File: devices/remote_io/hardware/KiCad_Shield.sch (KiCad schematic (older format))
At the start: 72 parts, among them IC1 ATECC508A, J1 Conn_01x04_Male, P1 Power, P2 Analog, P3 Digital, P4 Digital, P5 CONN_1, P6 CONN_1, P7 CONN_1, P8 CONN_1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

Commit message: Added JLCPCB
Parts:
- D1, D2, D3, D4: LCSC (none) -> C397049
- Q1, Q3: LCSC (none) -> C82045
- Q2, Q4: LCSC (none) -> C411721
- R1, R10, R2, R3, R4, R5, R6, R7, R8, R9: LCSC (none) -> C21189
- R11, R12, R13, R14, R28, R30, R31, R34, R36, R38, R40, R42, R45, R46, R48, R49, R50, R52: LCSC (none) -> C25804
- R21, R22, R23, R24: LCSC (none) -> C21190
- R47, R51: LCSC (none) -> C4190
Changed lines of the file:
@@
 EESchema Schematic File Version 4
-LIBS:KiCad_Shield-cache
 EELAYER 30 0
 EELAYER END
@@
 F 2 "Resistor_SMD:R_0603_1608Metric" V 6830 1900 50  0001 C CNN
 F 3 "" H 6900 1900 50  0000 C CNN
+F 4 "C25804" V 6900 1900 50  0001 C CNN "LCSC"
 	1    6900 1900
 	0    1    1    0
@@
 F 2 "Resistor_SMD:R_0603_1608Metric" V 6830 2500 50  0001 C CNN
 F 3 "" H 6900 2500 50  0000 C CNN
+F 4 "C25804" V 6900 2500 50  0001 C CNN "LCSC"
 	1    6900 2500
 	0    1    1    0
@@
 F 2 "Resistor_SMD:R_0603_1608Metric" V 6830 2900 50  0001 C CNN
 F 3 "" H 6900 2900 50  0000 C CNN
+F 4 "C25804" V 6900 2900 50  0001 C CNN "LCSC"
 	1    6900 2900
 	0    1    1    0
@@
 F 2 "Resistor_SMD:R_0603_1608Metric" V 6830 3750 50  0001 C CNN
 F 3 "" H 6900 3750 50  0000 C CNN
+F 4 "C25804" V 6900 3750 50  0001 C CNN "LCSC"
 	1    6900 3750
 	0    1    1    0
@@
 F 2 "Resistor_SMD:R_0603_1608Metric" V 6830 4350 50  0001 C CNN
 F 3 "" H 6900 4350 50  0000 C CNN
+F 4 "C25804" V 6900 4350 50  0001 C CNN "LCSC"
 	1    6900 4350
 	0    1    1    0
@@
 F 2 "Resistor_SMD:R_0603_1608Metric" V 6830 4950 50  0001 C CNN
 F 3 "" H 6900 4950 50  0000 C CNN
+F 4 "C25804" V 6900 4950 50  0001 C CNN "LCSC"
 	1    6900 4950
 	0    1    1    0
@@
 F 2 "Resistor_SMD:R_0603_1608Metric" V 6830 5600 50  0001 C CNN
 F 3 "" H 6900 5600 50  0000 C CNN
+F 4 "C25804" V 6900 5600 50  0001 C CNN "LCSC"
 	1    6900 5600
 	0    1    1    0
@@
 F 2 "Resistor_SMD:R_0603_1608Metric" V 6830 6200 50  0001 C CNN
 F 3 "" H 6900 6200 50  0000 C CNN
+F 4 "C25804" V 6900 6200 50  0001 C CNN "LCSC"
 	1    6900 6200
 	0    1    1    0
@@
 F 2 "Resistor_SMD:R_0603_1608Metric" V 2830 2300 50  0001 C CNN
 F 3 "" H 2900 2300 50  0000 C CNN
+F 4 "C21189" V 2900 2300 50  0001 C CNN "LCSC"
 	1    2900 2300
 	0    1    1    0
@@
 F 2 "Resistor_SMD:R_0603_1608Metric" V 2830 2200 50  0001 C CNN
 F 3 "" H 2900 2200 50  0000 C CNN
+F 4 "C21189" V 2900 2200 50  0001 C CNN "LCSC"
 	1    2900 2200
 	0    1    1    0
@@
 F 2 "Resistor_SMD:R_0603_1608Metric" V 2830 2100 50  0001 C CNN
 F 3 "" H 2900 2100 50  0000 C CNN
+F 4 "C21189" V 2900 2100 50  0001 C CNN "LCSC"
 	1    2900 2100
 	0    1    1    0
@@
 F 2 "Resistor_SMD:R_0603_1608Metric" V 2830 2000 50  0001 C CNN
 F 3 "" H 2900 2000 50  0000 C CNN
+F 4 "C21189" V 2900 2000 50  0001 C CNN "LCSC"
 	1    2900 2000
 	0    1    1    0
@@
 F 2 "Resistor_SMD:R_0603_1608Metric" V 2830 1900 50  0001 C CNN
 F 3 "" H 2900 1900 50  0000 C CNN
+F 4 "C21189" V 2900 1900 50  0001 C CNN "LCSC"
 	1    2900 1900
 	0    1    1    0
@@
 F 2 "Resistor_SMD:R_0603_1608Metric" V 2830 1800 50  0001 C CNN
 F 3 "" H 2900 1800 50  0000 C CNN
+F 4 "C21189" V 2900 1800 50  0001 C CNN "LCSC"
 	1    2900 1800
 	0    1    1    0
@@
 F 2 "Resistor_SMD:R_0603_1608Metric" V 2830 1700 50  0001 C CNN
 F 3 "" H 2900 1700 50  0000 C CNN
+F 4 "C21189" V 2900 1700 50  0001 C CNN "LCSC"
 	1    2900 1700
 	0    1    1    0
@@
 F 2 "Resistor_SMD:R_0603_1608Metric" V 2830 1600 50  0001 C CNN
 F 3 "" H 2900 1600 50  0000 C CNN
+F 4 "C21189" V 2900 1600 50  0001 C CNN "LCSC"
 	1    2900 1600
 	0    1    1    0
@@
 F 2 "Resistor_SMD:R_0603_1608Metric" V 2830 1500 50  0001 C CNN
 F 3 "" H 2900 1500 50  0000 C CNN
+F 4 "C21189" V 2900 1500 50  0001 C CNN "LCSC"
 	1    2900 1500
 	0    1    1    0
@@
 F 2 "Resistor_SMD:R_0603_1608Metric" V 2830 1400 50  0001 C CNN
 F 3 "" H 2900 1400 50  0000 C CNN
+F 4 "C21189" V 2900 1400 50  0001 C CNN "LCSC"
 	1    2900 1400
 	0    1    1    0
@@
 F 2 "LED_SMD:LED_0603_1608Metric" H 9000 5750 50  0001 C CNN
 F 3 "~" H 9000 5750 50  0001 C CNN
+F 4 "C397049" V 9000 5750 50  0001 C CNN "LCSC"
 	1    9000 5750
 	0    -1   -1   0
@@
 F 2 "Resistor_SMD:R_0603_1608Metric_Pad1.05x0.95mm_HandSolder" V 8930 5350 50  0001 C CNN
 F 3 "" H 9000 5350 50  0000 C CNN
+F 4 "C21190" V 9000 5350 50  0001 C CNN "LCSC"
 	1    9000 5350
 	-1   0    0    1
@@
 F 2 "LED_SMD:LED_0603_1608Metric" H 9400 5750 50  0001 C CNN
 F 3 "~" H 9400 5750 50  0001 C CNN
+F 4 "C397049" V 9400 5750 50  0001 C CNN "LCSC"
 	1    9400 5750
 	0    -1   -1   0
@@
 F 2 "Resistor_SMD:R_0603_1608Metric_Pad1.05x0.95mm_HandSolder" V 9330 5350 50  0001 C CNN
 F 3 "" H 9400 5350 50  0000 C CNN
+F 4 "C21190" V 9400 5350 50  0001 C CNN "LCSC"
 	1    9400 5350
 	-1   0    0    1
@@
 F 2 "LED_SMD:LED_0603_1608Metric" H 9750 5750 50  0001 C CNN
 F 3 "~" H 9750 5750 50  0001 C CNN
+F 4 "C397049" V 9750 5750 50  0001 C CNN "LCSC"
 	1    9750 5750
 	0    -1   -1   0
@@
 F 2 "Resistor_SMD:R_0603_1608Metric_Pad1.05x0.95mm_HandSolder" V 9680 5350 50  0001 C CNN
 F 3 "" H 9750 5350 50  0000 C CNN
+F 4 "C21190" V 9750 5350 50  0001 C CNN "LCSC"
 	1    9750 5350
 	-1   0    0    1
@@
 F 2 "LED_SMD:LED_0603_1608Metric" H 10150 5750 50  0001 C CNN
 F 3 "~" H 10150 5750 50  0001 C CNN
+F 4 "C397049" V 10150 5750 50  0001 C CNN "LCSC"
 	1    10150 5750
 	0    -1   -1   0
@@
 F 2 "Resistor_SMD:R_0603_1608Metric_Pad1.05x0.95mm_HandSolder" V 10080 5350 50  0001 C CNN
 F 3 "" H 10150 5350 50  0000 C CNN
+F 4 "C21190" V 10150 5350 50  0001 C CNN "LCSC"
 	1    10150 5350
 	-1   0    0    1
@@
 F 2 "Resistor_SMD:R_0603_1608Metric" V 980 7000 50  0001 C CNN
 F 3 "" H 1050 7000 50  0000 C CNN
+F 4 "C25804" V 1050 7000 50  0001 C CNN "LCSC"
 	1    1050 7000
 	0    -1   -1   0
@@
 F 2 "Resistor_SMD:R_0603_1608Metric" V 1830 6250 50  0001 C CNN
 F 3 "" H 1900 6250 50  0000 C CNN
+F 4 "C4190" V 1900 6250 50  0001 C CNN "LCSC"
 	1    1900 6250
 	0    -1   -1   0
@@
 F 2 "Resistor_SMD:R_0603_1608Metric" V 1530 6450 50  0001 C CNN
 F 3 "" H 1600 6450 50  0000 C CNN
+F 4 "C25804" V 1600 6450 50  0001 C CNN "LCSC"
 	1    1600 6450
 	1    0    0    -1
@@
 F 2 "Resistor_SMD:R_0603_1608Metric" V 2330 7150 50  0001 C CNN
 F 3 "" H 2400 7150 50  0000 C CNN
+F 4 "C25804" V 2400 7150 50  0001 C CNN "LCSC"
 	1    2400 7150
 	1    0    0    -1
@@
 F 2 "Resistor_SMD:R_0603_1608Metric" V 3930 6950 50  0001 C CNN
 F 3 "" H 4000 6950 50  0000 C CNN
+F 4 "C25804" V 4000 6950 50  0001 C CNN "LCSC"
 	1    4000 6950
 	0    -1   -1   0
@@
 F 2 "Resistor_SMD:R_0603_1608Metric" V 4780 6200 50  0001 C CNN
 F 3 "" H 4850 6200 50  0000 C CNN
+F 4 "C4190" V 4850 6200 50  0001 C CNN "LCSC"
 	1    4850 6200
 	0    -1   -1   0
@@
 F 2 "Resistor_SMD:R_0603_1608Metric" V 4480 6400 50  0001 C CNN
 F 3 "" H 4550 6400 50  0000 C CNN
+F 4 "C25804" V 4550 6400 50  0001 C CNN "LCSC"
 	1    4550 6400
 	1    0    0    -1
@@
 F 2 "Resistor_SMD:R_0603_1608Metric" V 5280 7100 50  0001 C CNN
 F 3 "" H 5350 7100 50  0000 C CNN
+F 4 "C25804" V 5350 7100 50  0001 C CNN "LCSC"
 	1    5350 7100
 	1    0    0    -1
@@
 F 2 "Package_TO_SOT_SMD:SOT-23" H 2500 6175 50  0001 L CIN
 F 3 "http://www.farnell.com/datasheets/1835997.pdf" H 2300 6250 50  0001 L CNN
+F 4 "C411721" H 2300 6250 50  0001 C CNN "LCSC"
 	1    2300 6250
 	1    0    0    1
@@
 F 2 "Package_TO_SOT_SMD:SOT-23" H 1700 6925 50  0001 L CIN
 F 3 "https://www.fairchildsemi.com/datasheets/BS/BSS138.pdf" H 1500 7000 50  0001 L CNN
+F 4 "C82045" H 1500 7000 50  0001 C CNN "LCSC"
 	1    1500 7000
 	1    0    0    -1
@@
 F 2 "Package_TO_SOT_SMD:SOT-23" H 4650 6875 50  0001 L CIN
 F 3 "https://www.fairchildsemi.com/datasheets/BS/BSS138.pdf" H 4450 6950 50  0001 L CNN
+F 4 "C82045" H 4450 6950 50  0001 C CNN "LCSC"
 	1    4450 6950
 	1    0    0    -1
@@
 F 2 "Package_TO_SOT_SMD:SOT-23" H 5450 6125 50  0001 L CIN
 F 3 "http://www.farnell.com/datasheets/1835997.pdf" H 5250 6200 50  0001 L CNN
+F 4 "C411721" H 5250 6200 50  0001 C CNN "LCSC"
 	1    5250 6200
 	1    0    0    1
@@
 F 2 "Resistor_SMD:R_0603_1608Metric" V 1530 5950 50  0001 C CNN
 F 3 "" H 1600 5950 50  0000 C CNN
+F 4 "C25804" V 1600 5950 50  0001 C CNN "LCSC"
 	1    1600 5950
 	1    0    0    -1
@@
 F 2 "Resistor_SMD:R_0603_1608Metric" V 4480 5900 50  0001 C CNN
 F 3 "" H 4550 5900 50  0000 C CNN
+F 4 "C25804" V 4550 5900 50  0001 C CNN "LCSC"
 	1    4550 5900
 	1    0    0    -1
@@
 F 2 "Resistor_SMD:R_0603_1608Metric" V 630 7300 50  0001 C CNN
 F 3 "" H 700 7300 50  0000 C CNN
+F 4 "C25804" V 700 7300 50  0001 C CNN "LCSC"
 	1    700  7300
 	1    0    0    -1
@@
 F 2 "Resistor_SMD:R_0603_1608Metric" V 3580 7250 50  0001 C CNN
 F 3 "" H 3650 7250 50  0000 C CNN
+F 4 "C25804" V 3650 7250 50  0001 C CNN "LCSC"
 	1    3650 7250
 	1    0    0    -1

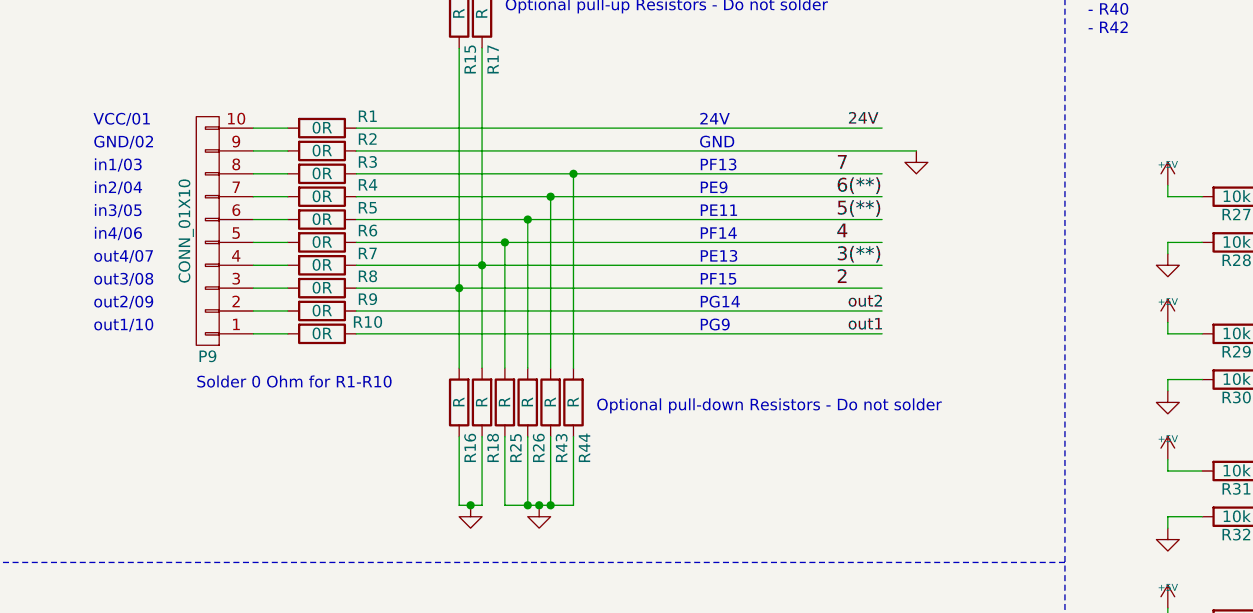
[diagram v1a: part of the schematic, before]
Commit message: Updated the Pull down Resistor in the schematic
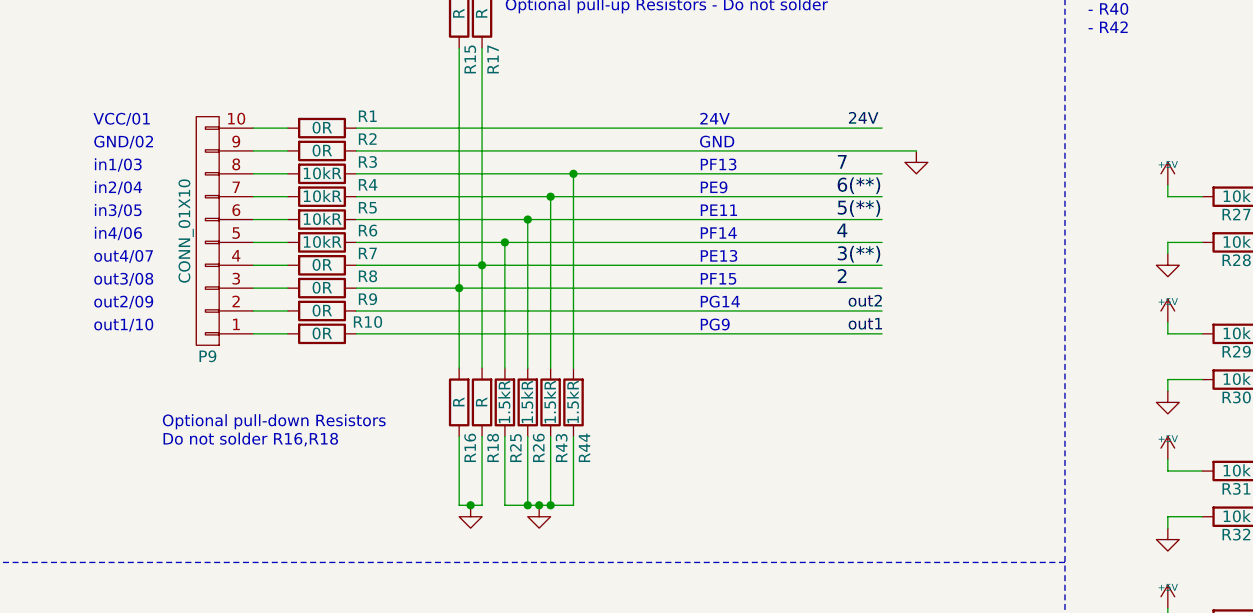
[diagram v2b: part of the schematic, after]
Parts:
- R25, R26, R43, R44: value R -> 1.5kR
- R3, R4, R5, R6: value 0R -> 10kR
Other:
- note added: "Optional pull-down Resistors\nDo not solder R16,R18"
- note removed: "Optional pull-down Resistors - Do not solder"
- note removed: "Solder 0 Ohm for R1-R10"
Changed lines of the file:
@@
 P 2900 1900
 F 0 "R6" V 2850 2100 50  0000 C CNN
-F 1 "0R" V 2900 1900 50  0000 C CNN
+F 1 "10kR" V 2900 1900 50  0000 C CNN
 F 2 "Resistor_SMD:R_0603_1608Metric" V 2830 1900 50  0001 C CNN
 F 3 "" H 2900 1900 50  0000 C CNN
@@
 P 2900 1800
 F 0 "R5" V 2850 2000 50  0000 C CNN
-F 1 "0R" V 2900 1800 50  0000 C CNN
+F 1 "10kR" V 2900 1800 50  0000 C CNN
 F 2 "Resistor_SMD:R_0603_1608Metric" V 2830 1800 50  0001 C CNN
 F 3 "" H 2900 1800 50  0000 C CNN
@@
 P 2900 1700
 F 0 "R4" V 2850 1900 50  0000 C CNN
-F 1 "0R" V 2900 1700 50  0000 C CNN
+F 1 "10kR" V 2900 1700 50  0000 C CNN
 F 2 "Resistor_SMD:R_0603_1608Metric" V 2830 1700 50  0001 C CNN
 F 3 "" H 2900 1700 50  0000 C CNN
@@
 P 2900 1600
 F 0 "R3" V 2850 1800 50  0000 C CNN
-F 1 "0R" V 2900 1600 50  0000 C CNN
+F 1 "10kR" V 2900 1600 50  0000 C CNN
 F 2 "Resistor_SMD:R_0603_1608Metric" V 2830 1600 50  0001 C CNN
 F 3 "" H 2900 1600 50  0000 C CNN
@@
 	1    2900 1400
 	0    1    1    0
-$EndComp
-$Comp
-L KiCad_Shield-rescue:R-device R16
-U 1 1 5B29A3EF
-P 3500 2600
-F 0 "R16" V 3450 2800 50  0000 C CNN
-F 1 "R" V 3500 2600 50  0000 C CNN
-F 2 "Resistor_SMD:R_0603_1608Metric" V 3430 2600 50  0001 C CNN
-F 3 "" H 3500 2600 50  0000 C CNN
-	1    3500 2600
-	-1   0    0    1
-$EndComp
-$Comp
-L KiCad_Shield-rescue:R-device R18
-U 1 1 5B29A3F5
-P 3600 2600
-F 0 "R18" V 3550 2800 50  0000 C CNN
-F 1 "R" V 3600 2600 50  0000 C CNN
-F 2 "Resistor_SMD:R_0603_1608Metric" V 3530 2600 50  0001 C CNN
-F 3 "" H 3600 2600 50  0000 C CNN
-	1    3600 2600
-	-1   0    0    1
 $EndComp
 $Comp
@@
 Wire Wire Line
 	7050 6200 7500 6200
-Wire Wire Line
-	3500 3050 3500 2750
 Wire Wire Line
 	2750 2300 2600 2300
@@
 Wire Wire Line
 	2750 1900 2600 1900
-Wire Wire Line
-	3600 3050 3600 2750
 Wire Wire Line
 	3600 750  3500 750
@@
 	3500 2100 5350 2100
 $Comp
-L KiCad_Shield-rescue:R-device R25
-U 1 1 5C67E2DE
-P 3700 2600
-F 0 "R25" V 3650 2800 50  0000 C CNN
-F 1 "R" V 3700 2600 50  0000 C CNN
-F 2 "Resistor_SMD:R_0603_1608Metric" V 3630 2600 50  0001 C CNN
-F 3 "" H 3700 2600 50  0000 C CNN
-	1    3700 2600
-	-1   0    0    1
-$EndComp
-$Comp
-L KiCad_Shield-rescue:R-device R26
-U 1 1 5C67E2E4
-P 3800 2600
-F 0 "R26" V 3750 2800 50  0000 C CNN
-F 1 "R" V 3800 2600 50  0000 C CNN
-F 2 "Resistor_SMD:R_0603_1608Metric" V 3730 2600 50  0001 C CNN
-F 3 "" H 3800 2600 50  0000 C CNN
-	1    3800 2600
-	-1   0    0    1
-$EndComp
-$Comp
-L KiCad_Shield-rescue:R-device R43
-U 1 1 5C67E2EA
-P 3900 2600
-F 0 "R43" V 3850 2800 50  0000 C CNN
-F 1 "R" V 3900 2600 50  0000 C CNN
-F 2 "Resistor_SMD:R_0603_1608Metric" V 3830 2600 50  0001 C CNN
-F 3 "" H 3900 2600 50  0000 C CNN
-	1    3900 2600
-	-1   0    0    1
-$EndComp
-$Comp
-L KiCad_Shield-rescue:R-device R44
-U 1 1 5C67E2F0
-P 4000 2600
-F 0 "R44" V 3950 2800 50  0000 C CNN
-F 1 "R" V 4000 2600 50  0000 C CNN
-F 2 "Resistor_SMD:R_0603_1608Metric" V 3930 2600 50  0001 C CNN
-F 3 "" H 4000 2600 50  0000 C CNN
-	1    4000 2600
-	-1   0    0    1
-$EndComp
-Wire Wire Line
-	3700 3050 3800 3050
-Wire Wire Line
-	3700 3050 3700 2750
-Wire Wire Line
-	3800 2750 3800 3050
-Connection ~ 3800 3050
-Wire Wire Line
-	3900 3050 3900 2750
-Connection ~ 3900 3050
-Wire Wire Line
-	4000 3050 4000 2750
-$Comp
 L KiCad_Shield-rescue:GND-power #PWR0103
 U 1 1 5C67E2FD
@@
 $EndComp
 Connection ~ 3850 3050
-Wire Wire Line
-	3800 3050 3850 3050
-Wire Wire Line
-	3900 3050 4000 3050
-Wire Wire Line
-	3850 3050 3900 3050
 Wire Wire Line
 	3700 2450 3700 1900
@@
 	1    0    0    -1
 $EndComp
-Text Notes 2350 2550 0    50   ~ 0
-Solder 0 Ohm for R1-R10
 Wire Notes Line
 	11200 4450 8500 4450
@@
 Text Notes 3700 900  0    50   ~ 0
 Optional pull-up Resistors - Do not solder
-Text Notes 4100 2650 0    50   ~ 0
-Optional pull-down Resistors - Do not solder
 Connection ~ 7050 1900
 Connection ~ 7050 2500
@@
 Text Notes 7400 1000 0    50   ~ 0
 For 2. Board populate only:\n- R32\n- R33\n- R38\n- R40\n- R42
+Wire Wire Line
+	3850 3050 3900 3050
+Wire Wire Line
+	3900 3050 4000 3050
+Connection ~ 3900 3050
+Connection ~ 3800 3050
+Wire Wire Line
+	3800 3050 3850 3050
+Wire Wire Line
+	3700 3050 3800 3050
+Text Notes 2200 2800 0    50   ~ 0
+Optional pull-down Resistors\nDo not solder R16,R18
+Wire Wire Line
+	4000 3050 4000 2750
+Wire Wire Line
+	3900 3050 3900 2750
+Wire Wire Line
+	3800 2750 3800 3050
+Wire Wire Line
+	3700 3050 3700 2750
+$Comp
+L KiCad_Shield-rescue:R-device R44
+U 1 1 5C67E2F0
+P 4000 2600
+F 0 "R44" V 3950 2800 50  0000 C CNN
+F 1 "1.5kR" V 4000 2600 50  0000 C CNN
+F 2 "Resistor_SMD:R_0603_1608Metric" V 3930 2600 50  0001 C CNN
+F 3 "" H 4000 2600 50  0000 C CNN
+	1    4000 2600
+	-1   0    0    1
+$EndComp
+$Comp
+L KiCad_Shield-rescue:R-device R43
+U 1 1 5C67E2EA
+P 3900 2600
+F 0 "R43" V 3850 2800 50  0000 C CNN
+F 1 "1.5kR" V 3900 2600 50  0000 C CNN
+F 2 "Resistor_SMD:R_0603_1608Metric" V 3830 2600 50  0001 C CNN
+F 3 "" H 3900 2600 50  0000 C CNN
+	1    3900 2600
+	-1   0    0    1
+$EndComp
+$Comp
+L KiCad_Shield-rescue:R-device R26
+U 1 1 5C67E2E4
+P 3800 2600
+F 0 "R26" V 3750 2800 50  0000 C CNN
+F 1 "1.5kR" V 3800 2600 50  0000 C CNN
+F 2 "Resistor_SMD:R_0603_1608Metric" V 3730 2600 50  0001 C CNN
+F 3 "" H 3800 2600 50  0000 C CNN
+	1    3800 2600
+	-1   0    0    1
+$EndComp
+$Comp
+L KiCad_Shield-rescue:R-device R25
+U 1 1 5C67E2DE
+P 3700 2600
+F 0 "R25" V 3650 2800 50  0000 C CNN
+F 1 "1.5kR" V 3700 2600 50  0000 C CNN
+F 2 "Resistor_SMD:R_0603_1608Metric" V 3630 2600 50  0001 C CNN
+F 3 "" H 3700 2600 50  0000 C CNN
+	1    3700 2600
+	-1   0    0    1
+$EndComp
+Wire Wire Line
+	3600 3050 3600 2750
+Wire Wire Line
+	3500 3050 3500 2750
+$Comp
+L KiCad_Shield-rescue:R-device R18
+U 1 1 5B29A3F5
+P 3600 2600
+F 0 "R18" V 3550 2800 50  0000 C CNN
+F 1 "R" V 3600 2600 50  0000 C CNN
+F 2 "Resistor_SMD:R_0603_1608Metric" V 3530 2600 50  0001 C CNN
+F 3 "" H 3600 2600 50  0000 C CNN
+	1    3600 2600
+	-1   0    0    1
+$EndComp
+$Comp
+L KiCad_Shield-rescue:R-device R16
+U 1 1 5B29A3EF
+P 3500 2600
+F 0 "R16" V 3450 2800 50  0000 C CNN
+F 1 "R" V 3500 2600 50  0000 C CNN
+F 2 "Resistor_SMD:R_0603_1608Metric" V 3430 2600 50  0001 C CNN
+F 3 "" H 3500 2600 50  0000 C CNN
+	1    3500 2600
+	-1   0    0    1
+$EndComp
 $EndSCHEMATC
